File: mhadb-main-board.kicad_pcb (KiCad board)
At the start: 2 copper layers, 110 parts, among them J1 Conn_01x04, J10 Conn_01x04_Pin, J2 Conn_01x04, J3 USB_C_Receptacle_USB2.0_14P, J4 Conn_01x02, J5 Conn_01x03, J6 Conn_01x03, J7 Conn_01x04, J8 Conn_01x04, J9 Conn_01x04_Pin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

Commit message: schem/pcb: fix XT30 polarity
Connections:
- J4 pad 1: +BATT -> BGND
- J4 pad 2: BGND -> +BATT
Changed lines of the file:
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@@
 			(remove_unused_layers no)
 			(roundrect_rratio 0.2)
-			(net 15 "+BATT")
+			(net 8 "BGND")
 			(pinfunction "Pin_1")
 			(pintype "passive")
@@
 			(layers "*.Cu" "*.Mask")
 			(remove_unused_layers no)
-			(net 8 "BGND")
+			(net 15 "+BATT")
 			(pinfunction "Pin_2")
 			(pintype "passive")

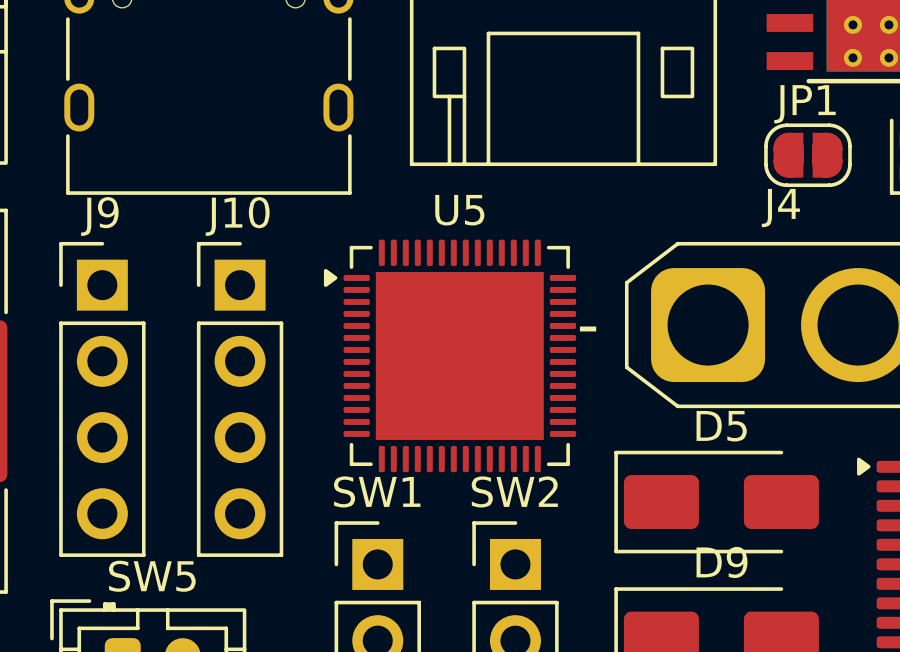
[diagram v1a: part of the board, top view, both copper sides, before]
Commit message: schem/pcb: changed esp32 footprint
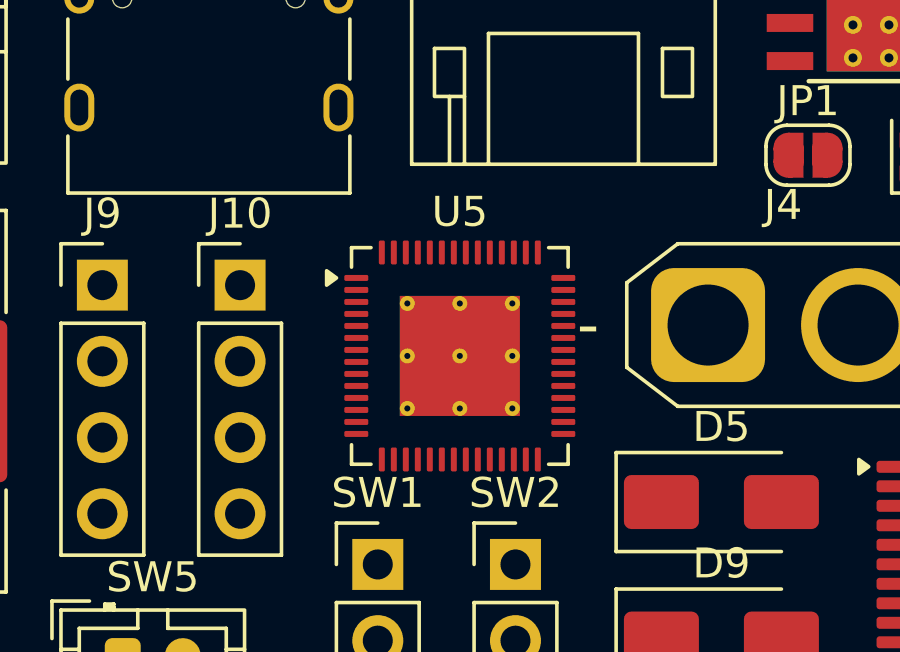
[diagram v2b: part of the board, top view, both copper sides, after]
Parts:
- U5: footprint Package_DFN_QFN:QFN-56-1EP_7x7mm_P0.4mm_EP5.6x5.6mm -> Package_DFN_QFN:QFN-56-1EP_7x7mm_P0.4mm_EP4x4mm_ThermalVias

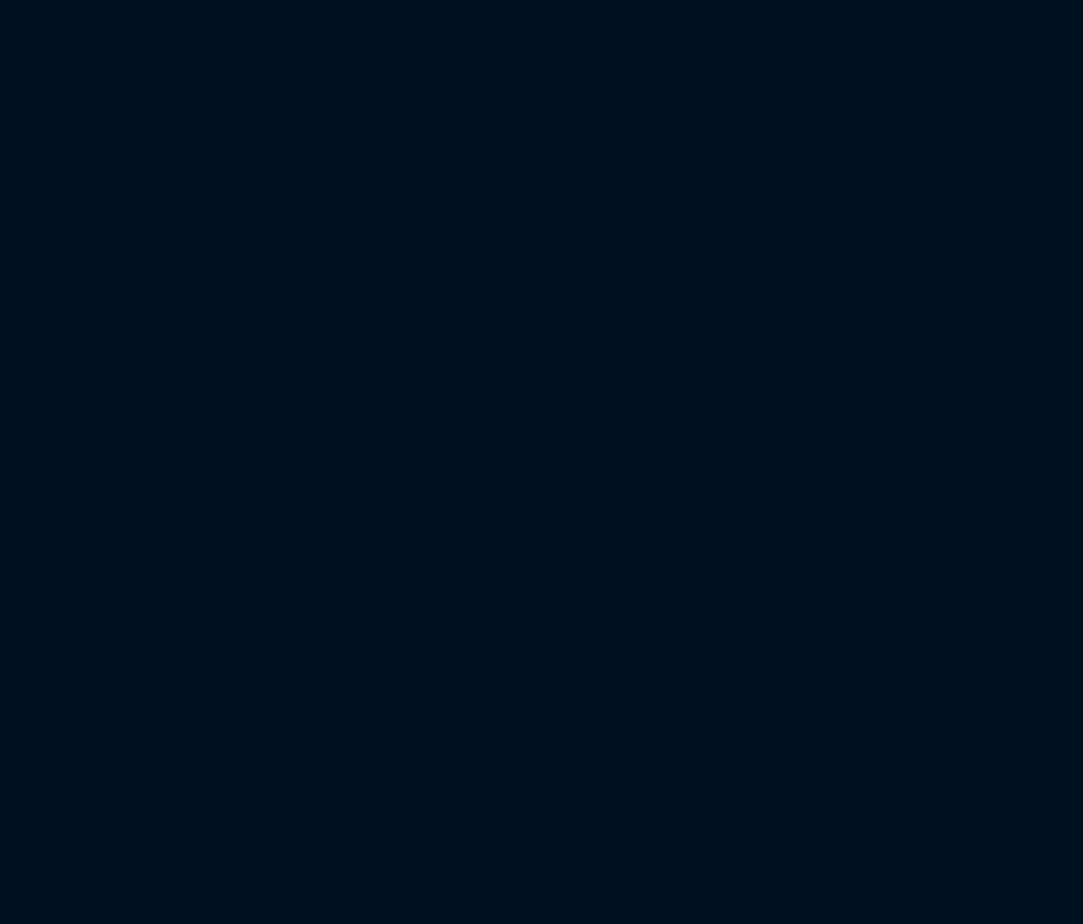
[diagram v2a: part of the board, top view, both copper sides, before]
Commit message: pcb: add board outline
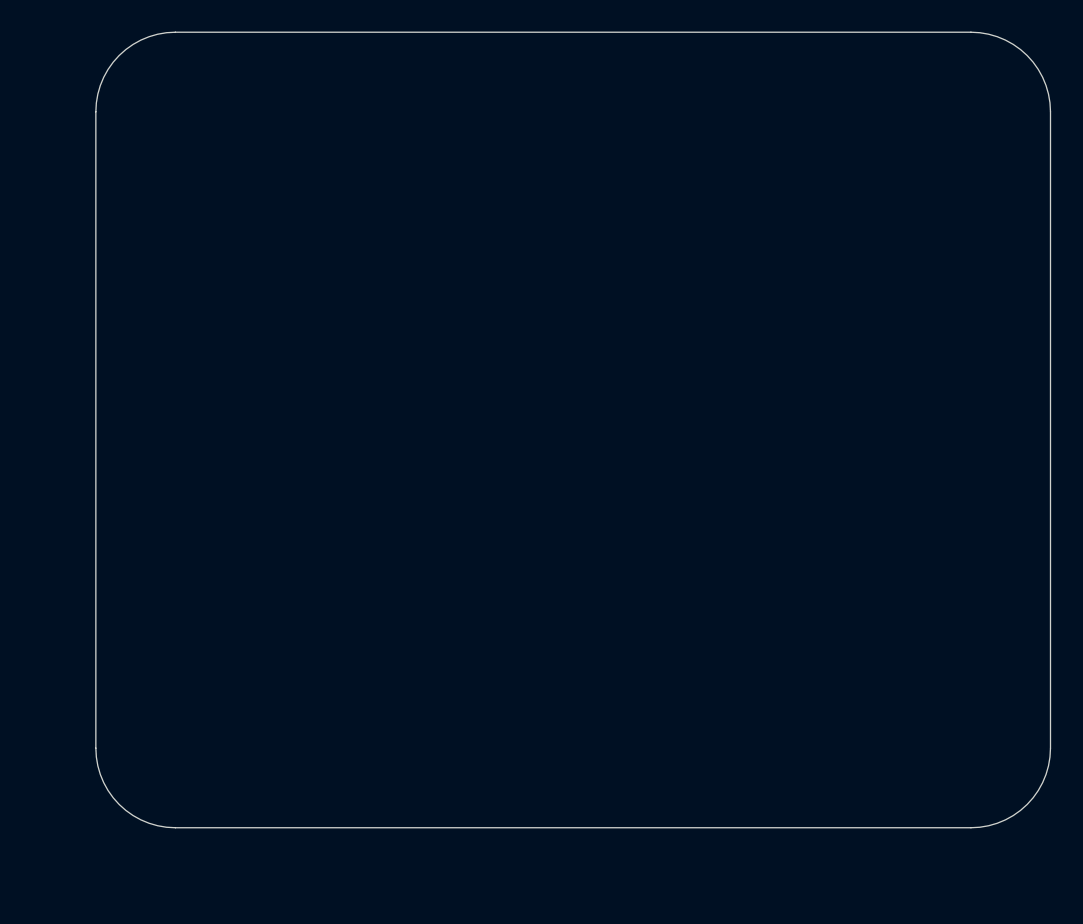
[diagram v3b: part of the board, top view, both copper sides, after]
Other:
- board outline added: 60 x 50 mm
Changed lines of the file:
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@@
 		)
+	)
+	(gr_arc
+		(start 155 50)
+		(mid 158.535534 51.464466)
+		(end 160 55)
+		(stroke
+			(width 0.05)
+			(type default)
+		)
+		(layer "Edge.Cuts")
+	)
+	(gr_line
+		(start 155 100)
+		(end 105 100)
+		(stroke
+			(width 0.05)
+			(type default)
+		)
+		(layer "Edge.Cuts")
+	)
+	(gr_arc
+		(start 105 100)
+		(mid 101.464466 98.535534)
+		(end 100 95)
+		(stroke
+			(width 0.05)
+			(type default)
+		)
+		(layer "Edge.Cuts")
+	)
+	(gr_line
+		(start 100 95)
+		(end 100 55)
+		(stroke
+			(width 0.05)
+			(type default)
+		)
+		(layer "Edge.Cuts")
+	)
+	(gr_arc
+		(start 100 55)
+		(mid 101.464466 51.464466)
+		(end 105 50)
+		(stroke
+			(width 0.05)
+			(type default)
+		)
+		(layer "Edge.Cuts")
+	)
+	(gr_line
+		(start 160 55)
+		(end 160 95)
+		(stroke
+			(width 0.05)
+			(type default)
+		)
+		(layer "Edge.Cuts")
+	)
+	(gr_arc
+		(start 160 95)
+		(mid 158.535534 98.535534)
+		(end 155 100)
+		(stroke
+			(width 0.05)
+			(type default)
+		)
+		(layer "Edge.Cuts")
+	)
+	(gr_line
+		(start 105 50)
+		(end 155 50)
+		(stroke
+			(width 0.05)
+			(type default)
+		)
+		(layer "Edge.Cuts")
 	)
 	(embedded_fonts no)

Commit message: schem/pcb: add mounting holes
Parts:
- added H1: MountingHole_Pad, GLCS:MountingHole_3.2mm_M3_DIN965_Pad_Thin, F.Cu at (110.0, 139.3)
- added H2: MountingHole_Pad, GLCS:MountingHole_3.2mm_M3_DIN965_Pad_Thin, F.Cu at (110.0, 145.9)
- added H3: MountingHole_Pad, GLCS:MountingHole_3.2mm_M3_DIN965_Pad_Thin, F.Cu at (110.0, 152.4)
- added H4: MountingHole_Pad, GLCS:MountingHole_3.2mm_M3_DIN965_Pad_Thin, F.Cu at (110.0, 159.0)

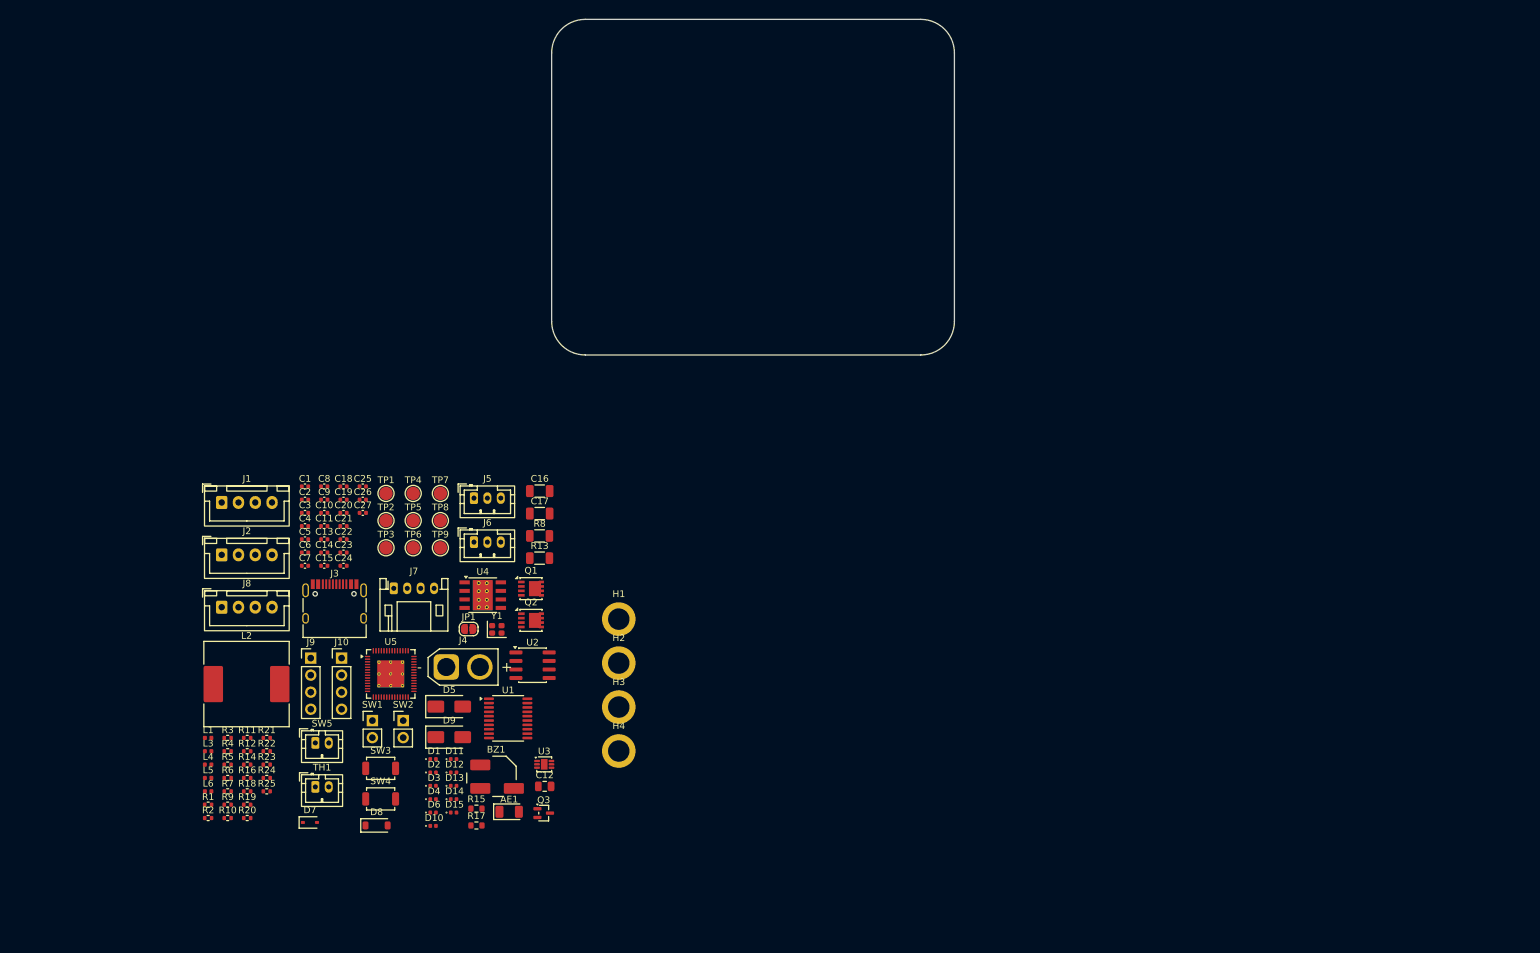
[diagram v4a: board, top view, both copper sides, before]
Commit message: pcb: refine layout of every block
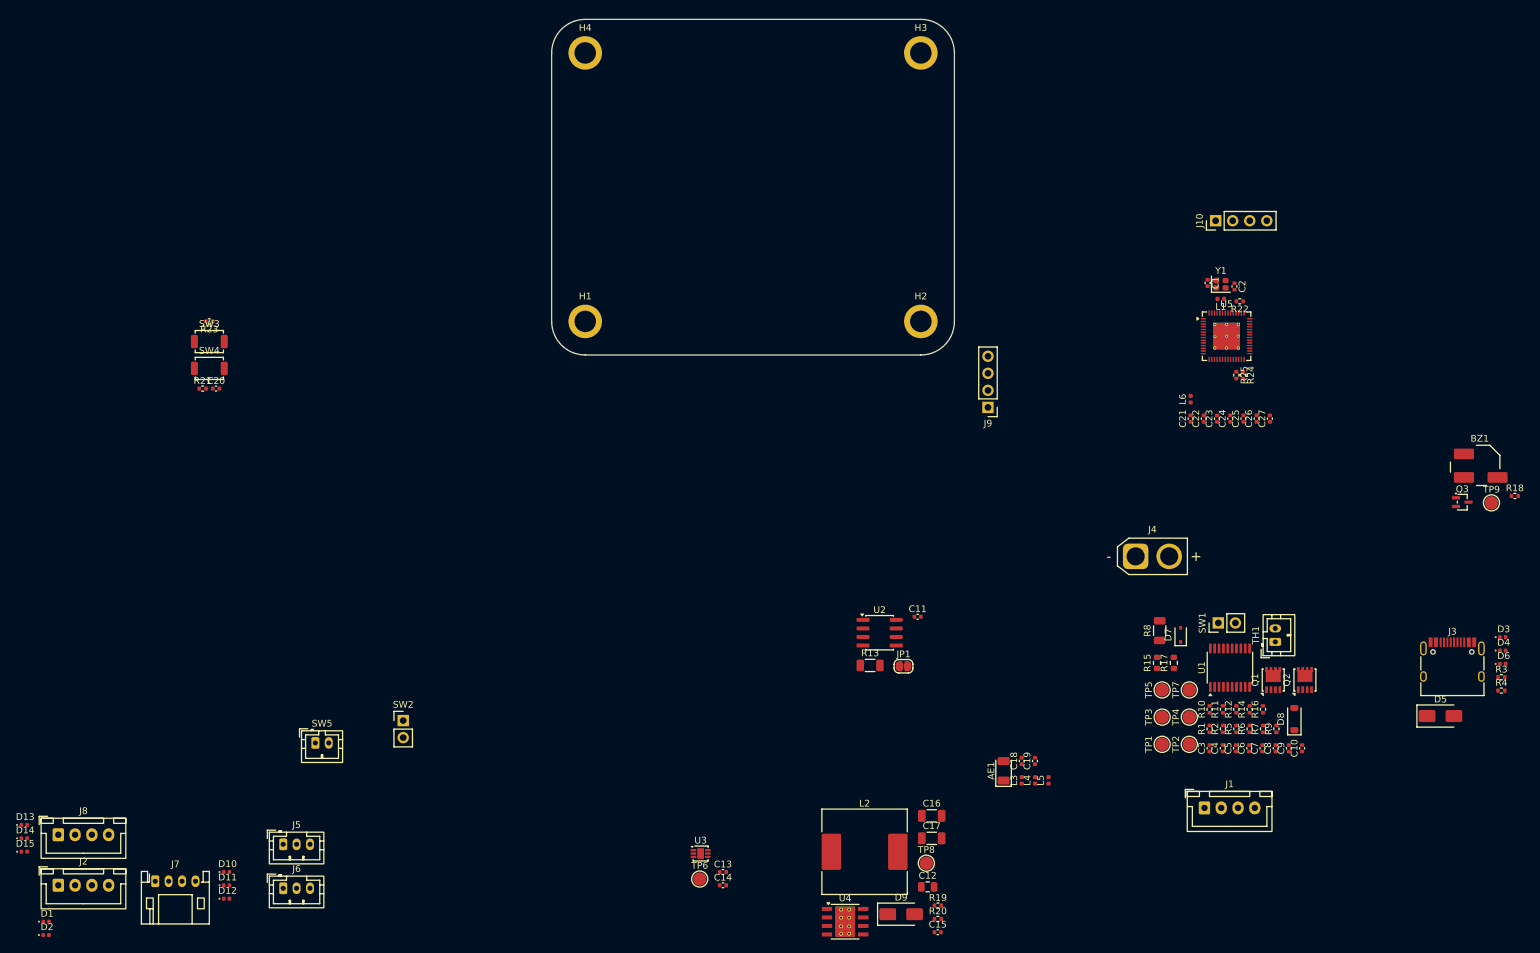
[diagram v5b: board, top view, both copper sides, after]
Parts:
- moved R18 193.9 mm to (243.5, 121.0)
- moved R3 190.0 mm to (241.5, 148.0)
- moved R4 190.0 mm to (241.5, 150.0)
- moved J3 166.8 mm to (234.2, 146.8)
- moved L1 164.4 mm to (199.7, 91.6), turned to 180 degrees
- moved D3 160.9 mm to (241.7, 142.0)
- moved D4 160.9 mm to (241.7, 144.0)
- moved D6 160.9 mm to (241.7, 146.0)
- moved R22 159.7 mm to (202.5, 92.0), turned to 180 degrees
- moved L6 157.6 mm to (195.2, 106.6), turned to 90 degrees
- moved R24 157.3 mm to (203.0, 103.0), turned to -90 degrees
- moved R25 157.2 mm to (202.0, 103.0), turned to -90 degrees
- moved TP9 156.7 mm to (240.0, 122.0)
- moved R9 156.6 mm to (208.0, 155.7), turned to 90 degrees
- moved R7 154.5 mm to (206.0, 155.7), turned to 90 degrees
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
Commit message: pcb: initial layout
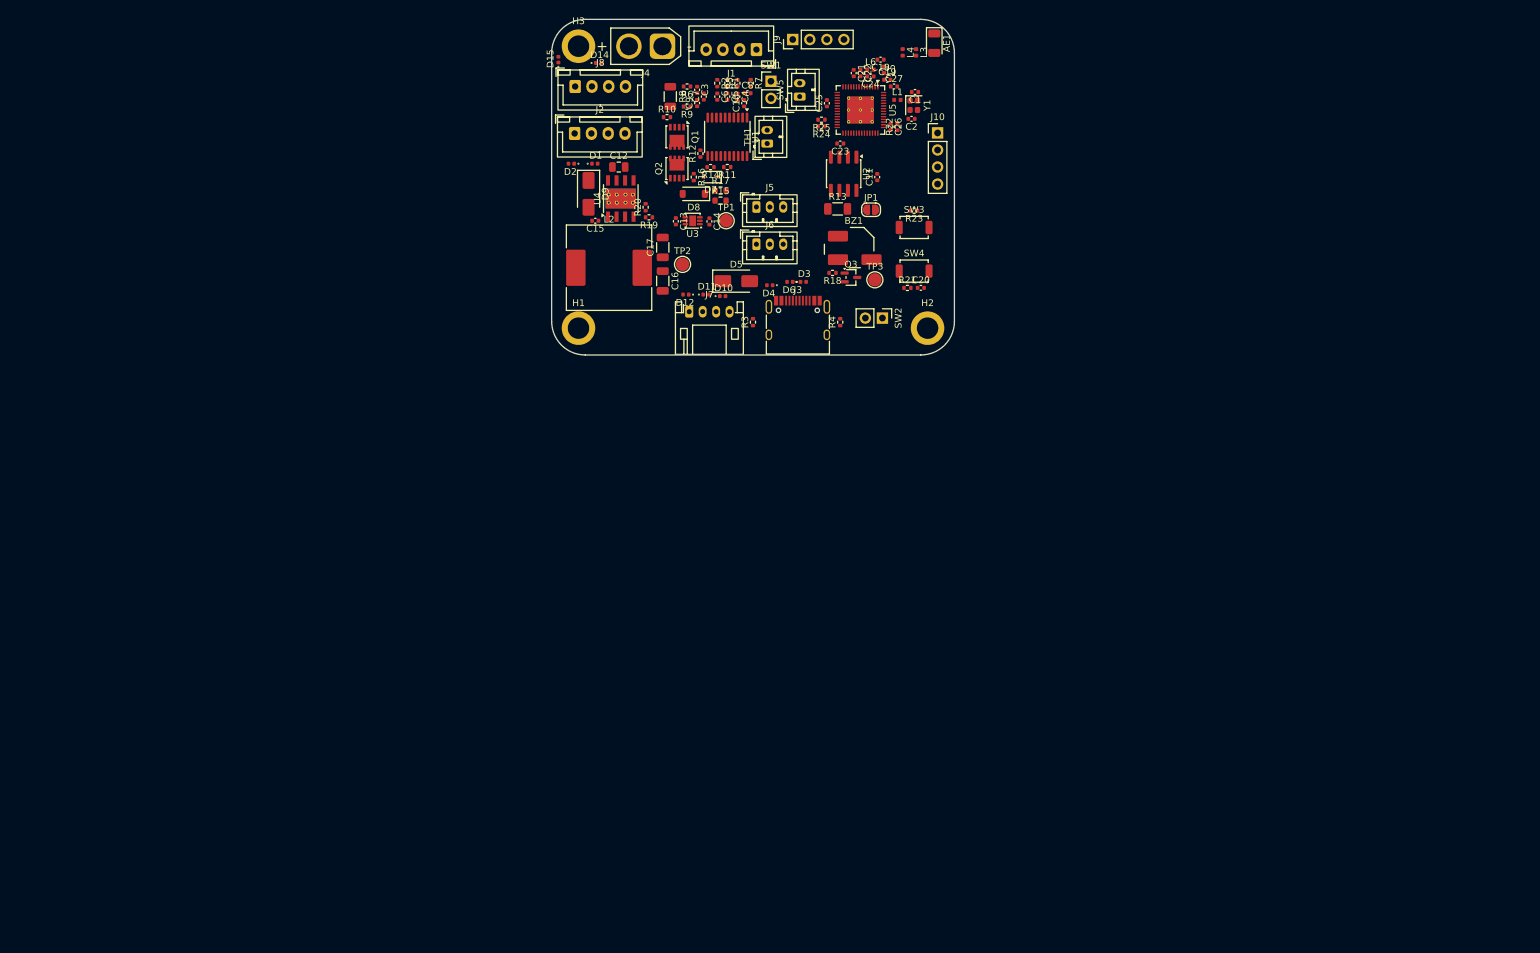
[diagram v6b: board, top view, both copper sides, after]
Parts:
- removed D13: H5VU10U, GLCS:Diode_DFN1006
- removed the H3 at (155.0, 55.0)
- removed the TP1 at (190.9, 158.0)
- removed the TP2 at (195.0, 158.0)
- removed the TP3 at (190.9, 153.9)
- removed TP4, TP5, TP7: TestPoint, TestPoint:TestPoint_Pad_D2.0mm
- moved D14 143.7 mm to (107.0, 56.5)
- moved D15 142.3 mm to (101.0, 56.0), turned to 90 degrees
- moved D1 139.4 mm to (106.4, 71.5)
- moved D2 139.0 mm to (102.9, 71.5), turned to 180 degrees
- moved J2 135.9 mm to (103.4, 67.0)
- moved J8 135.5 mm to (103.5, 60.0)
- moved J1 131.2 mm to (130.5, 54.5), turned to 180 degrees
- moved C9 130.4 mm to (121.7, 62.5)
- moved C7 127.9 mm to (122.7, 61.5)
- moved R9 127.7 mm to (120.2, 63.0), turned to 180 degrees
- moved R6 127.2 mm to (120.2, 60.0), turned to 180 degrees
- moved C10 127.1 mm to (128.7, 62.5)
- moved C8 125.4 mm to (129.2, 61.0), turned to 0 degrees
- moved C6 125.3 mm to (124.7, 61.5), turned to -90 degrees
- moved C3 124.3 mm to (121.7, 60.5), turned to -90 degrees
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- renumbered H4 to H3, TP6 to TP1, TP8 to TP2, TP9 to TP3
